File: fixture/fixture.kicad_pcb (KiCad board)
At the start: 2 copper layers, 100 x 100 mm, 48 parts, among them J1 Conn_Coaxial, J10 Conn_Coaxial, J11 Conn_Coaxial, J12 Conn_Coaxial, J13 Conn_Coaxial, J14 Conn_Coaxial, J15 Conn_Coaxial, J16 Conn_Coaxial, J17 Conn_Coaxial, J18 Conn_01x01, J19 Conn_01x01, J2 Conn_Coaxial, J20 Conn_01x01, J21 Conn_01x01, J22 Conn_Coaxial, J23 Conn_Coaxial, J24 Conn_Coaxial, J25 Conn_01x02, J26 Conn_01x01, J27 Conn_Coaxial, J28 Conn_01x02, J29 Conn_Coaxial, J3 Conn_Coaxial, J30 Conn_01x01, J31 Conn_01x01, J32 Conn_Coaxial, J33 Conn_01x01, J34 Conn_01x01, J35 Conn_01x01, J36 Conn_01x01, J37 Conn_01x01, J38 Conn_01x01, J39 Conn_01x01, J4 Conn_02x08_Counter_Clockwise, J40 Conn_Coaxial, J5 Conn_02x08_Counter_Clockwise, J6 Conn_Coaxial, J7 Conn_Coaxial, J8 Conn_Coaxial, J9 Conn_Coaxial

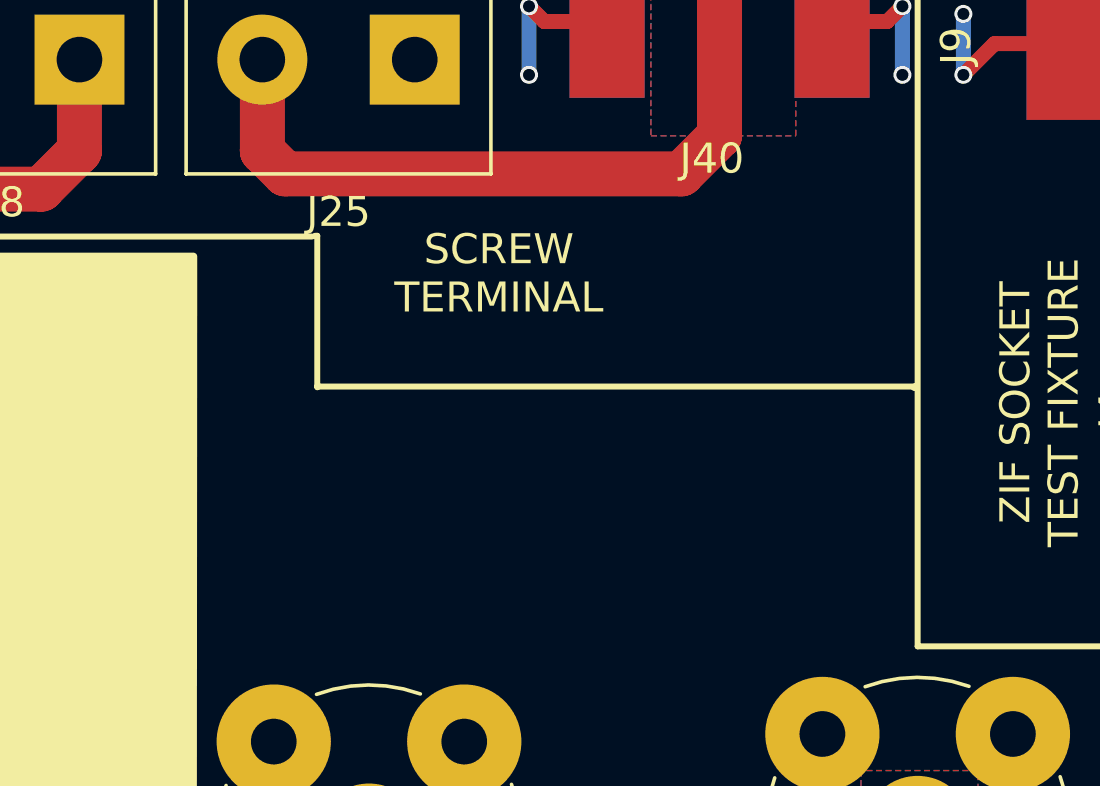
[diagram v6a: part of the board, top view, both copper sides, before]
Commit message: Added VNA-O-MIZER Logo
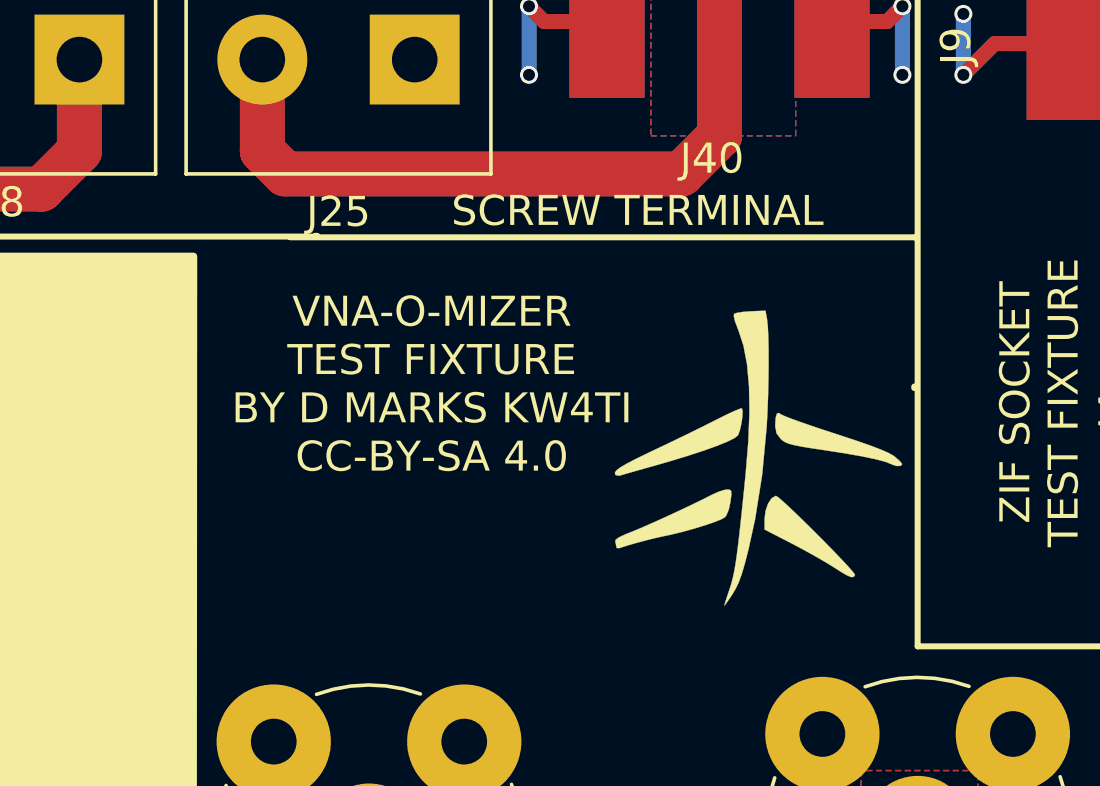
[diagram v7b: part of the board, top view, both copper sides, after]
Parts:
- added G***: LOGO, fixture:VNAOMizer, F.Cu at (101.9, 67.4)
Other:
- board text added: "VNA-O-MIZER TEST FIXTURE BY D MARKS KW4TI CC-BY-SA 4.0"
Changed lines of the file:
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@@
     (area 38.849999 37.934999 161.550001 161.625001)
     (thickness 1.6)
-    (drawings 53)
+    (drawings 54)
     (tracks 329)
     (zones 0)
-    (modules 48)
+    (modules 49)
     (nets 17)
   )
@@
   )
   (setup
-    (last_trace_width 1.5)
+    (last_trace_width 0.25)
     (user_trace_width 0.35)
     (user_trace_width 0.5)
@@
     (pad "" np_thru_hole circle (at 0 0) (size 1.5 1.5) (drill 1.5) (layers *.Cu *.Mask))
   )
+  (module fixture:VNAOMizer (layer F.Cu)
+    (at 101.875 67.375)
+    (fp_text reference G*** (at 0 0) (layer F.SilkS) hide
+      (effects (font (thickness 0.3)))
+    )
+    (fp_text value LOGO (at 0.75 0) (layer F.SilkS) hide
+      (effects (font (thickness 0.3)))
+    )
+    (fp_poly (pts (xy 0.293123 -4.621389) (xy 0.317894 -4.398101) (xy 0.334924 -4.059111) (xy 0.344295 -3.629613)
+      (xy 0.34609 -3.134799) (xy 0.340391 -2.599861) (xy 0.327282 -2.049993) (xy 0.306845 -1.510387)
+      (xy 0.281376 -1.040503) (xy 0.132851 0.549482) (xy -0.105598 2.051599) (xy -0.329137 3.068511)
+      (xy -0.44618 3.524507) (xy -0.548457 3.872163) (xy -0.646898 4.141893) (xy -0.752432 4.364109)
+      (xy -0.859182 4.543478) (xy -0.990915 4.742234) (xy -1.086976 4.877522) (xy -1.128467 4.922866)
+      (xy -1.128889 4.921308) (xy -1.107542 4.840305) (xy -1.050995 4.66136) (xy -0.970491 4.419781)
+      (xy -0.951308 4.363564) (xy -0.898844 4.199208) (xy -0.851171 4.020657) (xy -0.806283 3.813472)
+      (xy -0.76217 3.563215) (xy -0.716825 3.255448) (xy -0.668239 2.875732) (xy -0.614404 2.40963)
+      (xy -0.553313 1.842704) (xy -0.482956 1.160514) (xy -0.422889 0.564444) (xy -0.332038 -0.538475)
+      (xy -0.293424 -1.515472) (xy -0.307325 -2.371822) (xy -0.374021 -3.1128) (xy -0.49379 -3.743681)
+      (xy -0.666911 -4.269739) (xy -0.680017 -4.300431) (xy -0.776027 -4.552624) (xy -0.816049 -4.729629)
+      (xy -0.80382 -4.798291) (xy -0.705213 -4.833254) (xy -0.507852 -4.863601) (xy -0.254079 -4.882859)
+      (xy -0.248985 -4.883076) (xy 0.2416 -4.903612) (xy 0.293123 -4.621389)) (layer F.SilkS) (width 0.01))
+    (fp_poly (pts (xy 0.668263 1.317823) (xy 0.82314 1.450533) (xy 1.041855 1.651986) (xy 1.308286 1.906042)
+      (xy 1.606316 2.196557) (xy 1.919825 2.507389) (xy 2.232692 2.822398) (xy 2.5288 3.12544)
+      (xy 2.792028 3.400373) (xy 3.006256 3.631056) (xy 3.155366 3.801346) (xy 3.223238 3.895102)
+      (xy 3.225398 3.905751) (xy 3.182105 3.970047) (xy 3.099226 3.976528) (xy 2.956451 3.918004)
+      (xy 2.733471 3.787287) (xy 2.540815 3.663418) (xy 2.271595 3.49674) (xy 1.919779 3.292474)
+      (xy 1.529298 3.075503) (xy 1.144085 2.87071) (xy 1.112065 2.854184) (xy 0.211667 2.390755)
+      (xy 0.211667 2.035297) (xy 0.243772 1.767589) (xy 0.32785 1.526408) (xy 0.445544 1.34856)
+      (xy 0.578497 1.270853) (xy 0.593341 1.27) (xy 0.668263 1.317823)) (layer F.SilkS) (width 0.01))
+    (fp_poly (pts (xy -0.946216 1.065488) (xy -0.900925 1.10942) (xy -0.896299 1.223823) (xy -0.922406 1.442396)
+      (xy -0.924452 1.457488) (xy -0.981931 1.726207) (xy -1.064968 1.924752) (xy -1.10667 1.978735)
+      (xy -1.230238 2.049751) (xy -1.462247 2.143052) (xy -1.773553 2.249581) (xy -2.135011 2.360284)
+      (xy -2.517475 2.466105) (xy -2.891801 2.557989) (xy -3.139722 2.610395) (xy -3.407776 2.668996)
+      (xy -3.736706 2.750557) (xy -4.078508 2.84215) (xy -4.385181 2.930848) (xy -4.608723 3.003724)
+      (xy -4.630389 3.011827) (xy -4.715506 3.006539) (xy -4.727222 2.976652) (xy -4.750819 2.849293)
+      (xy -4.767361 2.799718) (xy -4.751137 2.730729) (xy -4.640454 2.649848) (xy -4.418805 2.54681)
+      (xy -4.255833 2.481694) (xy -3.959586 2.360263) (xy -3.572416 2.19175) (xy -3.129516 1.99238)
+      (xy -2.666076 1.778374) (xy -2.217289 1.565958) (xy -1.818347 1.371353) (xy -1.541823 1.23054)
+      (xy -1.318736 1.13034) (xy -1.1183 1.068245) (xy -1.042105 1.058333) (xy -0.946216 1.065488)) (layer F.SilkS) (width 0.01))
+    (fp_poly (pts (xy -0.542509 -1.64788) (xy -0.521421 -1.549341) (xy -0.530529 -1.363452) (xy -0.56247 -1.138882)
+      (xy -0.609884 -0.924303) (xy -0.665407 -0.768384) (xy -0.679048 -0.745207) (xy -0.798112 -0.65308)
+      (xy -1.042072 -0.532947) (xy -1.398515 -0.389323) (xy -1.855024 -0.226725) (xy -2.399185 -0.04967)
+      (xy -3.018582 0.137325) (xy -3.421944 0.252633) (xy -3.804445 0.360157) (xy -4.142102 0.455712)
+      (xy -4.410267 0.532274) (xy -4.584297 0.582817) (xy -4.636768 0.598905) (xy -4.747126 0.577683)
+      (xy -4.770388 0.551681) (xy -4.777941 0.491533) (xy -4.724056 0.417029) (xy -4.596658 0.320843)
+      (xy -4.38367 0.195646) (xy -4.073018 0.034112) (xy -3.652626 -0.171087) (xy -3.316111 -0.330735)
+      (xy -2.868776 -0.543522) (xy -2.396326 -0.771903) (xy -1.941683 -0.994892) (xy -1.54777 -1.191506)
+      (xy -1.367319 -1.283497) (xy -1.066596 -1.433976) (xy -0.812523 -1.552478) (xy -0.630213 -1.62791)
+      (xy -0.544776 -1.649177) (xy -0.542509 -1.64788)) (layer F.SilkS) (width 0.01))
+    (fp_poly (pts (xy 0.731539 -1.46223) (xy 0.818222 -1.415777) (xy 1.020676 -1.333993) (xy 1.319994 -1.223676)
+      (xy 1.69727 -1.091624) (xy 2.1336 -0.944634) (xy 2.54 -0.811992) (xy 3.1671 -0.606363)
+      (xy 3.667291 -0.433407) (xy 4.050033 -0.289514) (xy 4.324785 -0.171074) (xy 4.501006 -0.074478)
+      (xy 4.533195 -0.051462) (xy 4.689368 0.081748) (xy 4.784372 0.186969) (xy 4.797778 0.217595)
+      (xy 4.741426 0.270517) (xy 4.610175 0.272792) (xy 4.460733 0.22468) (xy 4.445 0.215962)
+      (xy 4.245346 0.135201) (xy 3.909109 0.045705) (xy 3.440487 -0.051644) (xy 2.843679 -0.155962)
+      (xy 2.222161 -0.251889) (xy 1.762746 -0.320933) (xy 1.421289 -0.377361) (xy 1.175812 -0.426708)
+      (xy 1.004335 -0.474508) (xy 0.884877 -0.526294) (xy 0.795458 -0.587601) (xy 0.758473 -0.620418)
+      (xy 0.608861 -0.816858) (xy 0.564488 -1.055794) (xy 0.564445 -1.065764) (xy 0.58005 -1.332126)
+      (xy 0.624665 -1.477904) (xy 0.694992 -1.495271) (xy 0.731539 -1.46223)) (layer F.SilkS) (width 0.01))
+  )
+  (gr_line (start 107.15 60.025) (end 107.15 60.05) (angle 90) (layer F.SilkS) (width 0.2))
+  (gr_line (start 86.275 60.025) (end 107.15 60.025) (angle 90) (layer F.SilkS) (width 0.2))
+  (gr_text "VNA-O-MIZER\nTEST FIXTURE\nBY D MARKS KW4TI\nCC-BY-SA 4.0" (at 91 64.925) (layer F.SilkS)
+    (effects (font (size 1 1) (thickness 0.15)))
+  )
   (gr_line (start 87.175 59.975) (end 87.1 59.975) (angle 90) (layer F.SilkS) (width 0.2))
-  (gr_line (start 87.175 65.025) (end 87.175 59.975) (angle 90) (layer F.SilkS) (width 0.2))
   (gr_line (start 107.075 65) (end 107.075 65.05) (angle 90) (layer F.SilkS) (width 0.2))
-  (gr_line (start 87.175 65) (end 107.075 65) (angle 90) (layer F.SilkS) (width 0.2))
   (gr_line (start 114.046 73.66) (end 141.732 73.66) (angle 90) (layer F.SilkS) (width 0.2))
   (gr_line (start 102.2604 118.1862) (end 102.5398 118.1862) (angle 90) (layer F.SilkS) (width 0.2))
@@
     (effects (font (size 1 1) (thickness 0.15)))
   )
-  (gr_text "SCREW\nTERMINAL\n" (at 93.23 61.23) (layer F.SilkS)
+  (gr_text "SCREW TERMINAL\n" (at 97.85 59.15) (layer F.SilkS)
     (effects (font (size 1 1) (thickness 0.15)))
   )

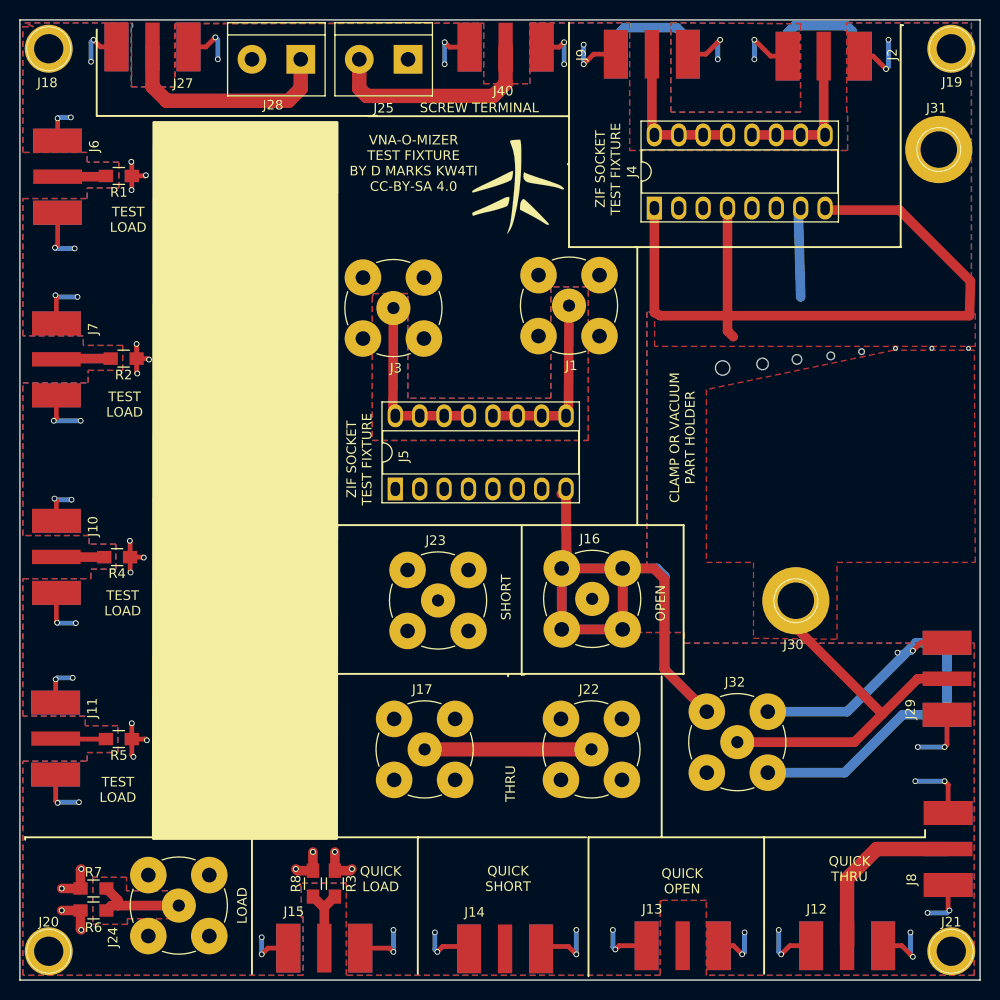
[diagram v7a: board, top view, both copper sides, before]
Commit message: Adds SD card support, which is mandatory.  Also changed firmware for new pinouts.
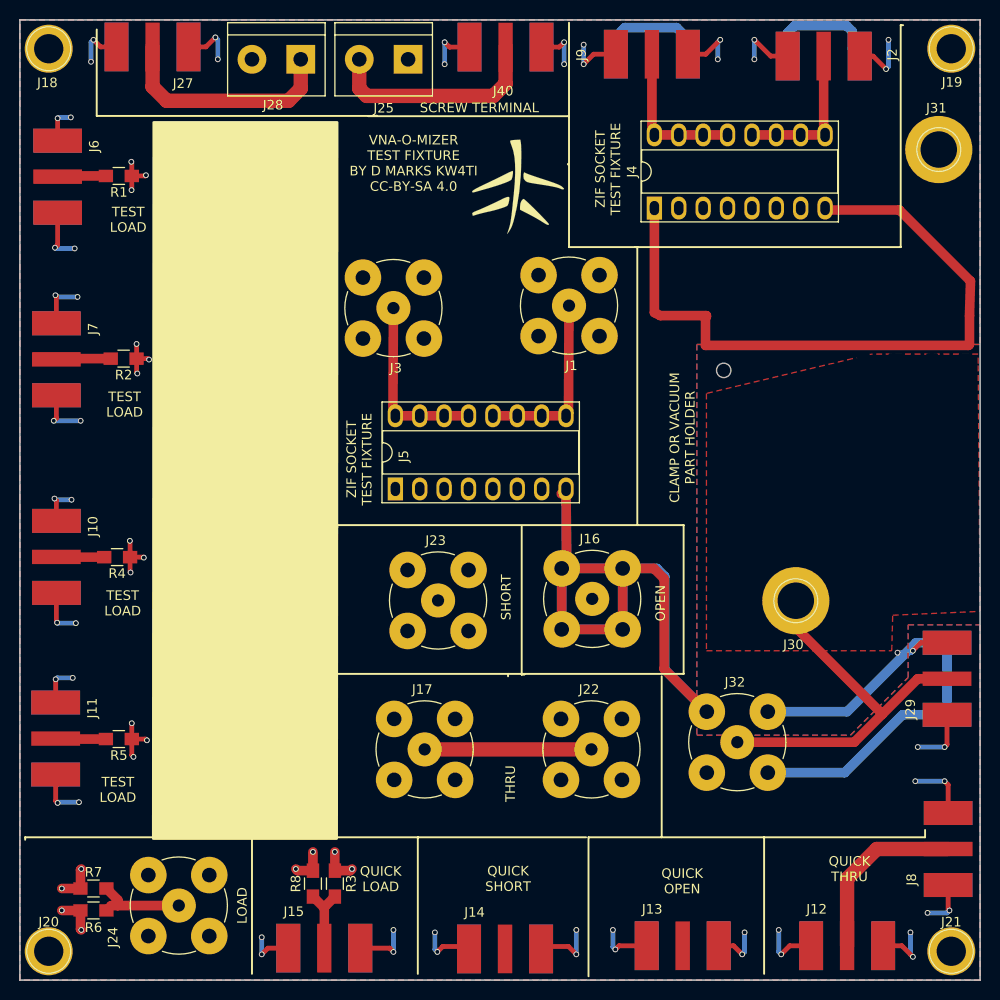
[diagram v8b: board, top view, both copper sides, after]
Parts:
- moved J37 0.75 mm to (148.5, 84.9)
- moved J34 0.70 mm to (145.0, 84.9)
- moved J39 0.70 mm to (141.2, 84.9)
- moved J38 0.47 mm to (137.8, 85.0)
- moved J33 0.31 mm to (134.5, 85.3)
- moved J35 0.29 mm to (131.1, 85.6)
- moved J26 0.27 mm to (123.3, 86.5)
- moved J36 0.18 mm to (127.4, 86.0)
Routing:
- net GND: track 462.4 -> 446.2 mm
